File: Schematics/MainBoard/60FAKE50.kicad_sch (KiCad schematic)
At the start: 12 parts, among them J7 Conn_01x02, Q2 IRLML6402, U10 FT245RNL

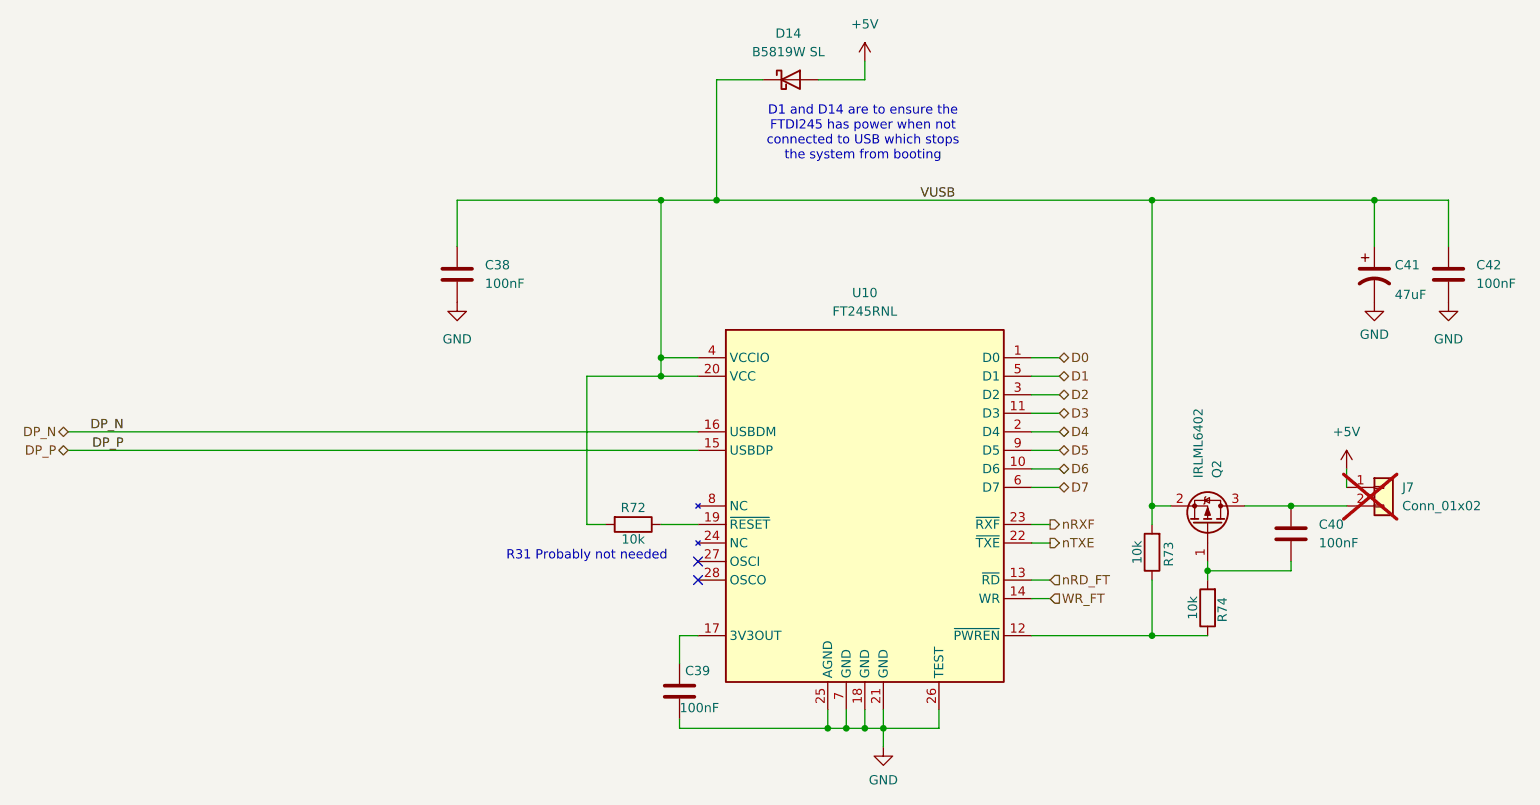
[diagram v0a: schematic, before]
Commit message: Updated USB wiring, moved key parts, increased board dimensions
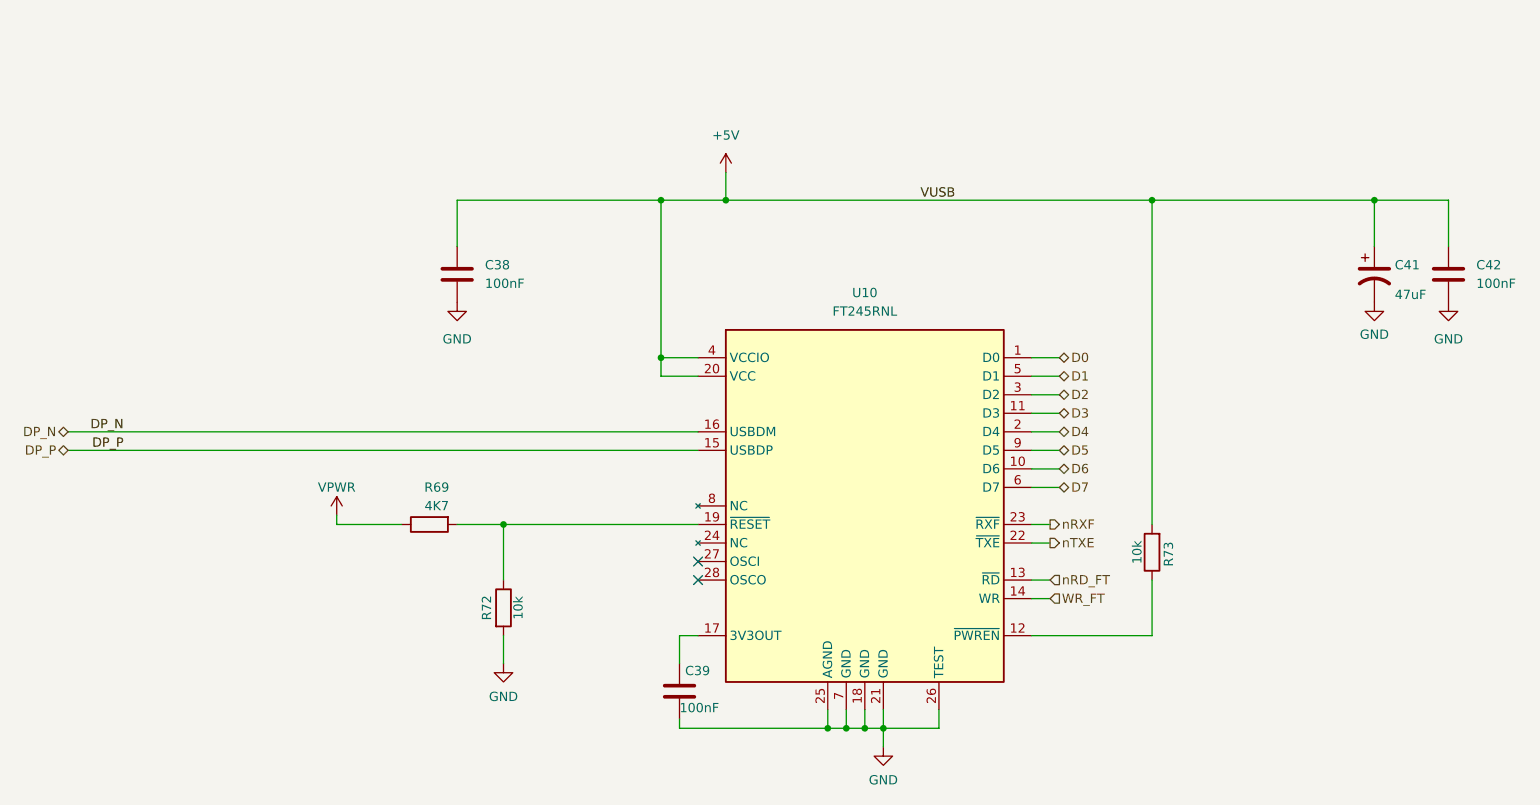
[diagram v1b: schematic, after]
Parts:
- removed C40: 100nF, Capacitor_SMD:C_0603_1608Metric, symbol Device:C
- removed D14: B5819W SL, Diode_SMD:D_SOD-123, symbol Device:D_Schottky
- removed J7: Conn_01x02, Connector_PinHeader_2.54mm:PinHeader_1x02_P2.54mm_Horizontal, symbol Connector_Generic:Conn_01x02
- removed Q2: IRLML6402, Package_TO_SOT_SMD:SOT-23, symbol Transistor_FET:IRLML6402
- removed R74: 10k, Resistor_SMD:R_0402_1005Metric, symbol Device:R
- added R69: 4K7, Resistor_SMD:R_0402_1005Metric, symbol Device:R
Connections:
- net +5V: now also C38.1, C41.1, C42.1, R73.2, U10.20 (VCC), U10.4 (VCCIO)
- net GND: now also R72.2
- net at R72.1, U10.19 (~{RESET}): now also R69.2
- removed net VUSB: C38.1, C41.1, C42.1, R72.2, R73.2, U10.20 (VCC), U10.4 (VCCIO)
- new net VPWR: R69.1
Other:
- note removed: "D1 and D14 are to ensure the FTDI245 has power when not connected to USB which stops the system from booting"
- note removed: "R31 Probably not needed"
- moved on the sheet: R72

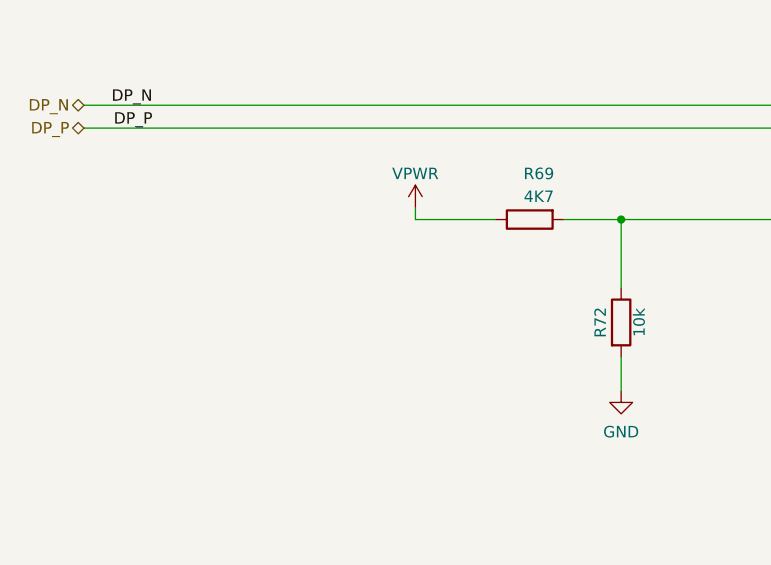
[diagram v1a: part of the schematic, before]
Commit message: Move to a single board for everything (keyboard and main board)
Aim is to save height
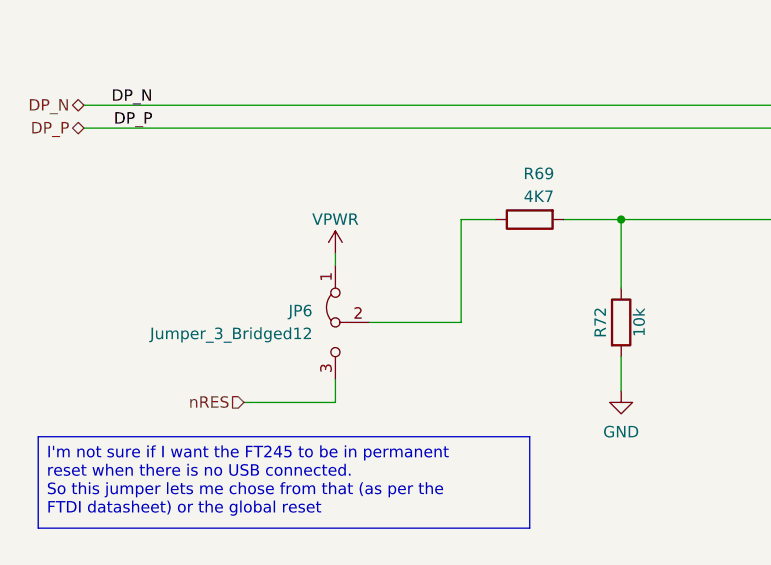
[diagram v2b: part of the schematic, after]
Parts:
- added JP6: Jumper_3_Bridged12, Jumper:SolderJumper-3_P1.3mm_Bridged2Bar12_RoundedPad1.0x1.5mm, symbol Jumper:Jumper_3_Bridged12
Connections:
- net VPWR: now also JP6.1 (A); no longer R69.1
- new net: JP6.2 (C), R69.1
- new net nRES: JP6.3 (B)
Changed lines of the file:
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@@
 	(generator_version "9.0")
 	(paper "A4")
+	(text_box "I'm not sure if I want the FT245 to be in permanent reset when there is no USB connected.\nSo this jumper lets me chose from that (as per the FTDI datasheet) or the global reset"
+		(exclude_from_sim no)
+		(at 48.26 128.27 0)
+		(size 54.61 10.16)
+		(margins 0.9525 0.9525 0.9525 0.9525)
+		(stroke
+			(width 0)
+			(type solid)
+		)
+		(fill
+			(type none)
+		)
+		(effects
+			(font
+				(size 1.27 1.27)
+			)
+			(justify left top)
+		)
+	)
 	(junction
 		(at 162.56 132.08)
@@
 	(wire
 		(pts
+			(xy 85.09 115.57) (xy 95.25 115.57)
+		)
+		(stroke
+			(width 0)
+			(type default)
+		)
+	)
+	(wire
+		(pts
 			(xy 143.51 55.88) (xy 143.51 59.69)
 		)
@@
 	(wire
 		(pts
+			(xy 71.12 124.46) (xy 81.28 124.46)
+		)
+		(stroke
+			(width 0)
+			(type default)
+		)
+	)
+	(wire
+		(pts
 			(xy 201.93 59.69) (xy 201.93 104.14)
 		)
@@
 	(wire
 		(pts
-			(xy 90.17 104.14) (xy 99.06 104.14)
-		)
-		(stroke
-			(width 0)
-			(type default)
-		)
-	)
-	(wire
-		(pts
 			(xy 106.68 104.14) (xy 113.03 104.14)
 		)
@@
 	(wire
 		(pts
-			(xy 90.17 104.14) (xy 90.17 102.87)
+			(xy 81.28 109.22) (xy 81.28 107.95)
 		)
 		(stroke
@@
 	(wire
 		(pts
+			(xy 95.25 115.57) (xy 95.25 104.14)
+		)
+		(stroke
+			(width 0)
+			(type default)
+		)
+	)
+	(wire
+		(pts
 			(xy 143.51 59.69) (xy 201.93 59.69)
 		)
@@
 	(wire
 		(pts
+			(xy 81.28 124.46) (xy 81.28 121.92)
+		)
+		(stroke
+			(width 0)
+			(type default)
+		)
+	)
+	(wire
+		(pts
 			(xy 165.1 132.08) (xy 172.72 132.08)
 		)
@@
 		(pts
 			(xy 162.56 132.08) (xy 165.1 132.08)
+		)
+		(stroke
+			(width 0)
+			(type default)
+		)
+	)
+	(wire
+		(pts
+			(xy 95.25 104.14) (xy 99.06 104.14)
 		)
 		(stroke
@@
 		)
 	)
+	(hierarchical_label "nRES"
+		(shape input)
+		(at 71.12 124.46 180)
+		(effects
+			(font
+				(size 1.27 1.27)
+			)
+			(justify right)
+		)
+	)
 	(hierarchical_label "D5"
 		(shape bidirectional)
@@
 			)
 			(justify left)
+		)
+	)
+	(symbol
+		(lib_id "Jumper:Jumper_3_Bridged12")
+		(at 81.28 115.57 90)
+		(mirror x)
+		(unit 1)
+		(exclude_from_sim no)
+		(in_bom no)
+		(on_board yes)
+		(dnp no)
+		(fields_autoplaced yes)
+		(property "Reference" "JP6"
+			(at 78.74 114.2999 90)
+			(effects
+				(font
+					(size 1.27 1.27)
+				)
+				(justify left)
+			)
+		)
+		(property "Value" "Jumper_3_Bridged12"
+			(at 78.74 116.8399 90)
+			(effects
+				(font
+					(size 1.27 1.27)
+				)
+				(justify left)
+			)
+		)
+		(property "Footprint" "Jumper:SolderJumper-3_P1.3mm_Bridged2Bar12_RoundedPad1.0x1.5mm"
+			(at 81.28 115.57 0)
+			(effects
+				(font
+					(size 1.27 1.27)
+				)
+				(hide yes)
+			)
+		)
+		(property "Datasheet" "~"
+			(at 81.28 115.57 0)
+			(effects
+				(font
+					(size 1.27 1.27)
+				)
+				(hide yes)
+			)
+		)
+		(property "Description" "Jumper, 3-pole, pins 1+2 closed/bridged"
+			(at 81.28 115.57 0)
+			(effects
+				(font
+					(size 1.27 1.27)
+				)
+				(hide yes)
+			)
+		)
+		(pin "3"
+		)
+		(pin "1"
+		)
+		(pin "2"
+		)
+		(instances
+			(project "MainBoard"
+				(path "/a2243a34-697c-4939-97f7-df548e421864/7bd40c60-bb79-47f8-862c-3602d4cfed76"
+					(reference "JP6")
+					(unit 1)
+				)
+			)
 		)
 	)
@@
 	(symbol
 		(lib_id "power:+3.3V")
-		(at 90.17 102.87 0)
+		(at 81.28 107.95 0)
 		(unit 1)
 		(exclude_from_sim no)
@@
 		(fields_autoplaced yes)
 		(property "Reference" "#PWR0153"
-			(at 90.17 106.68 0)
+			(at 81.28 111.76 0)
 			(effects
 				(font
@@
 		)
 		(property "Value" "VPWR"
-			(at 90.17 99.06 0)
+			(at 81.28 104.14 0)
 			(effects
 				(font
@@
 		)
 		(property "Footprint" ""
-			(at 90.17 102.87 0)
+			(at 81.28 107.95 0)
 			(effects
 				(font
@@
 		)
 		(property "Datasheet" ""
-			(at 90.17 102.87 0)
+			(at 81.28 107.95 0)
 			(effects
 				(font
@@
 		)
 		(property "Description" ""
-			(at 90.17 102.87 0)
-			(effects
-				(font
+			(at 81.28 107.95 0)
+			(effects
+				(font

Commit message: Work on PCB
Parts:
- C38, C42: footprint Capacitor_SMD:C_0805_2012Metric -> Capacitor_SMD:C_0402_1005Metric
- C39: footprint Capacitor_SMD:C_0603_1608Metric -> Capacitor_SMD:C_0402_1005Metric
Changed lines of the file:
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@@
 			)
 		)
-		(property "Footprint" "Capacitor_SMD:C_0603_1608Metric"
+		(property "Footprint" "Capacitor_SMD:C_0402_1005Metric"
 			(at 138.1252 130.81 0)
 			(effects
@@
 			)
 		)
-		(property "Footprint" "Capacitor_SMD:C_0805_2012Metric"
+		(property "Footprint" "Capacitor_SMD:C_0402_1005Metric"
 			(at 107.6452 73.66 0)
 			(effects
@@
 			)
 		)
-		(property "Footprint" "Capacitor_SMD:C_0805_2012Metric"
+		(property "Footprint" "Capacitor_SMD:C_0402_1005Metric"
 			(at 243.5352 73.66 0)
 			(effects

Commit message: Updates based on production files for JLC
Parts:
- C38, C42: LCSC C49678 -> C307331
- C39: LCSC C113803 -> C307331
- C41: LCSC C22367835 -> C96123
- JP6: LCSC (none) -> DNF; now not fitted
- R69: LCSC (none) -> C25900
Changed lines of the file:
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@@
 		(in_bom no)
 		(on_board yes)
-		(dnp no)
+		(dnp yes)
 		(fields_autoplaced yes)
 		(property "Reference" "JP6"
@@
 			)
 		)
+		(property "LCSC" "DNF"
+			(at 81.28 115.57 90)
+			(effects
+				(font
+					(size 1.27 1.27)
+				)
+				(hide yes)
+			)
+		)
 		(pin "3"
 		)
@@
 			)
 		)
-		(property "LCSC" "C113803"
+		(property "LCSC" "C307331"
 			(at 137.16 127 0)
 			(effects
@@
 			)
 		)
-		(property "LCSC" ""
+		(property "LCSC" "C25900"
 			(at 102.87 104.14 90)
 			(effects
@@
 			)
 		)
-		(property "LCSC" "C22367835"
+		(property "LCSC" "C96123"
 			(at 231.14 67.945 0)
 			(effects
@@
 			)
 		)
-		(property "LCSC" "C49678"
+		(property "LCSC" "C307331"
 			(at 106.68 69.85 0)
 			(effects
@@
 			)
 		)
-		(property "LCSC" "C49678"
+		(property "LCSC" "C307331"
 			(at 242.57 69.85 0)
 			(effects
